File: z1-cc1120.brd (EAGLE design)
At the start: 100 x 50 mm, 8 parts, among them X1 PN61729-S

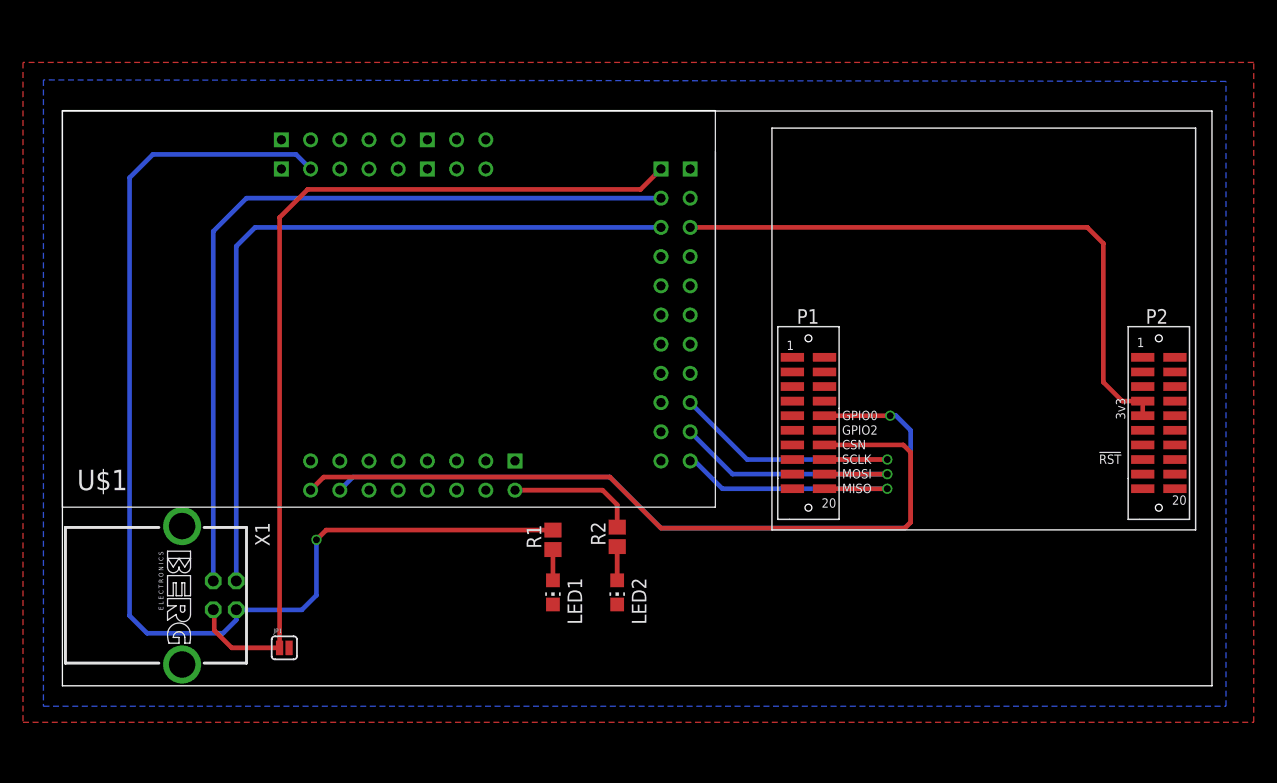
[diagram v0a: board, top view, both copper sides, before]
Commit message: Added silk screen info seperated usb_gnd & gnd added mounting holes
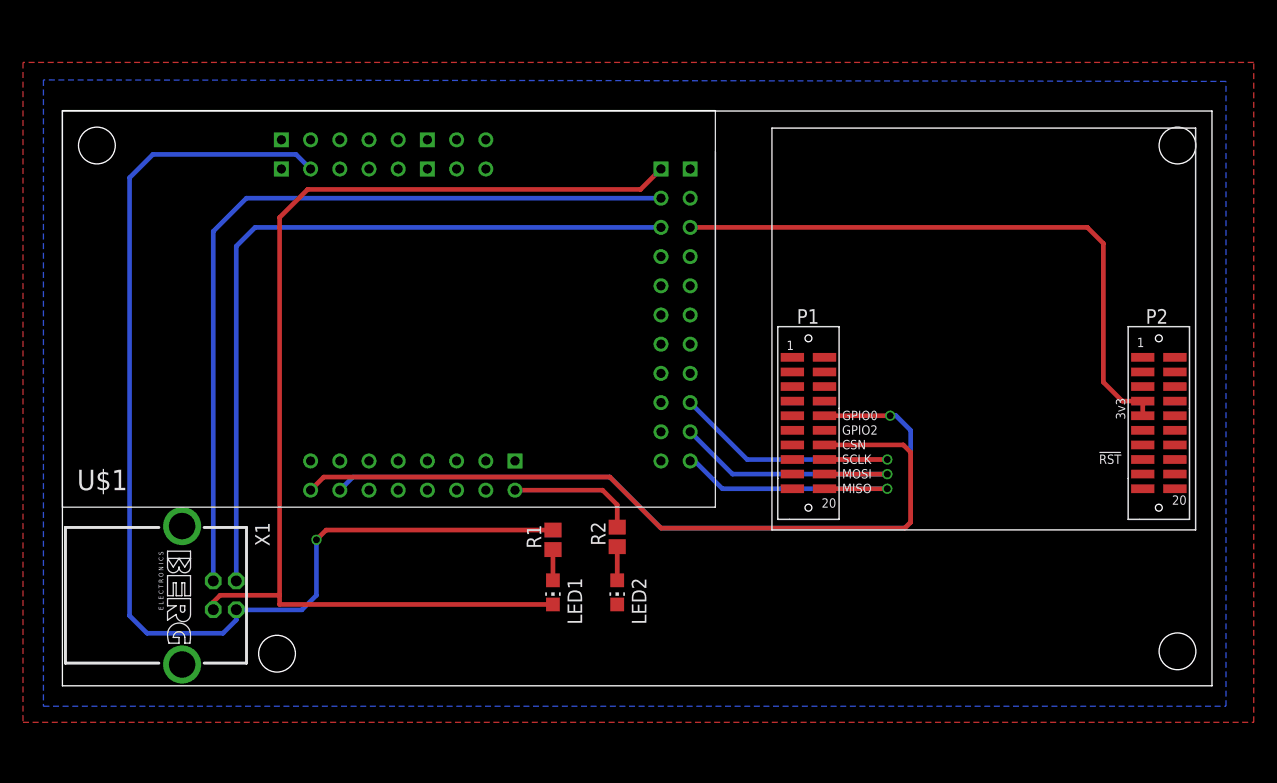
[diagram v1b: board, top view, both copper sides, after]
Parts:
- removed JP1: (no value), SparkFun-Passives:SJ_2S
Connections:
- net GND: no longer JP1.2, LED1.C
- net USB_GND: now also LED1.C; no longer JP1.1
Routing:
- net USB_GND: track 80.5 -> 99.0 mm
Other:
- board text added: "Mountain Sensing"
- board text added: "PJB"
- board text added: "Version 0.1"
- board text added: "Z1 - CC1120 Interface"
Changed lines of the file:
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@@
 <setting verticaltext="up"/>
 </settings>
-<grid distance="5" unitdist="mil" unit="mil" style="lines" multiple="1" display="no" altdistance="0.025" altunitdist="inch" altunit="inch"/>
+<grid distance="5" unitdist="mil" unit="mil" style="lines" multiple="1" display="yes" altdistance="0.025" altunitdist="inch" altunit="inch"/>
 <layers>
 <layer number="1" name="Top" color="4" fill="1" visible="yes" active="yes"/>
@@
 <layer number="43" name="vRestrict" color="2" fill="10" visible="yes" active="yes"/>
 <layer number="44" name="Drills" color="7" fill="1" visible="no" active="yes"/>
-<layer number="45" name="Holes" color="7" fill="1" visible="no" active="yes"/>
+<layer number="45" name="Holes" color="7" fill="1" visible="yes" active="yes"/>
 <layer number="46" name="Milling" color="3" fill="1" visible="no" active="yes"/>
 <layer number="47" name="Measures" color="7" fill="1" visible="no" active="yes"/>
@@
 <wire x1="100" y1="50" x2="0" y2="50" width="0" layer="20"/>
 <wire x1="0" y1="50" x2="0" y2="0" width="0" layer="20"/>
+<hole x="97" y="3" drill="3.2"/>
+<hole x="3" y="47" drill="3.2"/>
+<hole x="97" y="47" drill="3.2"/>
+<hole x="18.669" y="2.794" drill="3.2"/>
+<text x="61.087" y="9.652" size="1.778" layer="51">Z1 - CC1120 Interface</text>
+<text x="61.087" y="7.62" size="1.778" layer="51">Version 0.1</text>
+<text x="61.087" y="5.588" size="1.778" layer="51">Mountain Sensing</text>
+<text x="61.087" y="3.556" size="1.778" layer="51">PJB</text>
 </plain>
 <attributes>
@@
 <element name="LED1" library="led" package="CHIP-LED0805" value="" x="42.672" y="8.128" rot="R180"/>
 <element name="R1" library="resistor" package="R0805" value="150" x="42.672" y="12.7" rot="R90"/>
-<element name="JP1" library="SparkFun-Passives" package="SJ_2S" value="" x="19.304" y="3.302"/>
 </elements>
 <signals>
@@
 <contactref element="U$1" pad="B24" route="any" routetag="G$1.DGND"/>
 <contactref element="U$1" pad="C39" route="any" routetag="G$1.DGND"/>
-<contactref element="LED1" pad="C"/>
 <contactref element="LED2" pad="C"/>
-<contactref element="JP1" pad="2"/>
 <polygon width="0.4064" layer="16">
 <vertex x="-1.651" y="52.705"/>
@@
 <contactref element="U$1" pad="B17"/>
 <contactref element="X1" pad="4"/>
-<contactref element="JP1" pad="1"/>
-<wire x1="18.8921" y1="3.302" x2="18.8921" y2="40.7361" width="0.4064" layer="1"/>
 <wire x1="18.8921" y1="40.7361" x2="21.336" y2="43.18" width="0.4064" layer="1"/>
 <wire x1="21.336" y1="43.18" x2="50.292" y2="43.18" width="0.4064" layer="1"/>
 <wire x1="50.292" y1="43.18" x2="52.07" y2="44.958" width="0.4064" layer="1"/>
-<wire x1="18.8921" y1="3.302" x2="14.732" y2="3.302" width="0.4064" layer="1"/>
-<wire x1="14.732" y1="3.302" x2="13.208" y2="4.826" width="0.4064" layer="1"/>
-<wire x1="13.208" y1="4.826" x2="13.208" y2="6.54" width="0.4064" layer="1"/>
-<wire x1="13.208" y1="6.54" x2="13.124" y2="6.624" width="0.4064" layer="1"/>
+<contactref element="LED1" pad="C"/>
+<wire x1="18.8921" y1="40.7361" x2="18.8921" y2="7.874" width="0.4064" layer="1"/>
+<wire x1="18.8921" y1="7.874" x2="18.8921" y2="7.078" width="0.4064" layer="1"/>
+<wire x1="42.672" y1="7.078" x2="18.8921" y2="7.078" width="0.4064" layer="1"/>
+<wire x1="13.124" y1="6.624" x2="13.124" y2="7.282" width="0.4064" layer="1"/>
+<wire x1="13.124" y1="7.282" x2="13.716" y2="7.874" width="0.4064" layer="1"/>
+<wire x1="13.716" y1="7.874" x2="18.8921" y2="7.874" width="0.4064" layer="1"/>
 </signal>
 <signal name="RADIO_INT">

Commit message: Seperated radio gnd & vcc using inductor/cap network from z1 docs
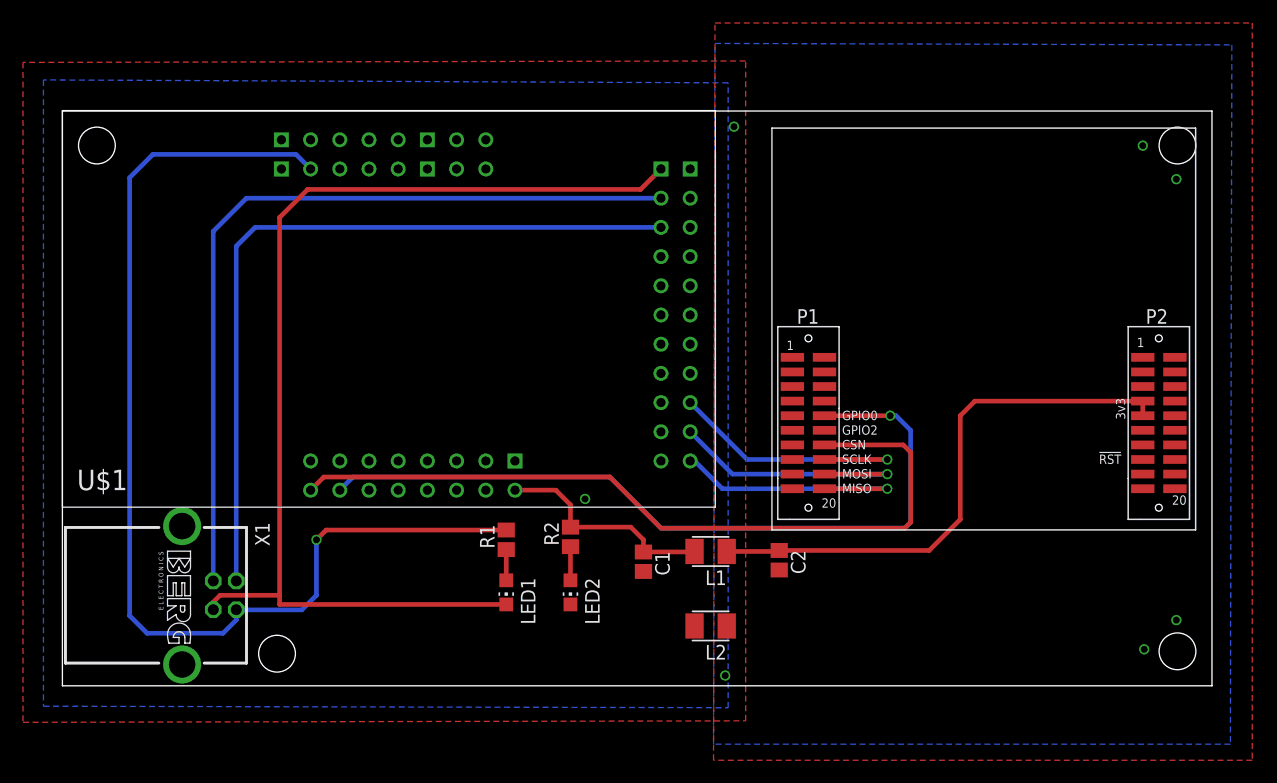
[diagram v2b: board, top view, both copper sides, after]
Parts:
- added C1, C2: 100nF, resistor:C0805
- added L1, L2: 10mH, resistor:L3230M
- moved LED1 4.06 mm to (38.6, 8.13)
- moved LED2 4.06 mm to (44.2, 8.13)
- moved R1 4.06 mm to (38.6, 12.7)
- moved R2 4.06 mm to (44.2, 13.0)
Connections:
- new net RADIO_3V3: C2.1, L1.1, U$2.3V3-1, U$2.3V3-2
- new net RADIO_GND: C2.2, L2.1, U$2.GND, U$2.GND1, U$2.GND2
- net GND: now also C1.2, L2.2; no longer U$2.GND, U$2.GND1, U$2.GND2
- net VCC_3V3: now also C1.1, L1.2; no longer U$2.3V3-1, U$2.3V3-2
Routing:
- net RADIO_3V3: track 0.00 -> 48.2 mm
- net VCC_3V3: track 65.3 -> 19.6 mm
- net USB_VCC: track 99.8 -> 95.7 mm
- net USB_GND: track 99.0 -> 95.0 mm
- added copper zone on layer 1, net RADIO_GND
- added copper zone on layer 16, net RADIO_GND
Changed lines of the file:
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@@
 <hole x="97" y="47" drill="3.2"/>
 <hole x="18.669" y="2.794" drill="3.2"/>
-<text x="61.087" y="9.652" size="1.778" layer="51">Z1 - CC1120 Interface</text>
-<text x="61.087" y="7.62" size="1.778" layer="51">Version 0.1</text>
-<text x="61.087" y="5.588" size="1.778" layer="51">Mountain Sensing</text>
-<text x="61.087" y="3.556" size="1.778" layer="51">PJB</text>
+<text x="72.898" y="9.779" size="1.778" layer="51">Z1 - CC1120 Interface</text>
+<text x="72.898" y="7.747" size="1.778" layer="51">Version 0.1</text>
+<text x="72.898" y="5.715" size="1.778" layer="51">Mountain Sensing</text>
+<text x="72.898" y="3.683" size="1.778" layer="51">PJB</text>
 </plain>
 <attributes>
@@
 <attribute name="OC_FARNELL" value="unknown" x="10.414" y="7.874" size="1.778" layer="27" rot="R270" display="off"/>
 </element>
-<element name="LED2" library="led" package="CHIP-LED0805" value="" x="48.26" y="8.128" rot="R180"/>
-<element name="R2" library="resistor" package="R0805" value="56" x="48.26" y="12.954" rot="R90"/>
-<element name="LED1" library="led" package="CHIP-LED0805" value="" x="42.672" y="8.128" rot="R180"/>
-<element name="R1" library="resistor" package="R0805" value="150" x="42.672" y="12.7" rot="R90"/>
+<element name="LED2" library="led" package="CHIP-LED0805" value="" x="44.196" y="8.128" rot="R180"/>
+<element name="R2" library="resistor" package="R0805" value="56" x="44.196" y="12.954" rot="R90"/>
+<element name="LED1" library="led" package="CHIP-LED0805" value="" x="38.608" y="8.128" rot="R180"/>
+<element name="R1" library="resistor" package="R0805" value="150" x="38.608" y="12.7" rot="R90"/>
+<element name="C1" library="resistor" package="C0805" value="100nF" x="50.546" y="10.795" rot="R270"/>
+<element name="C2" library="resistor" package="C0805" value="100nF" x="62.357" y="10.922" rot="R270"/>
+<element name="L1" library="resistor" package="L3230M" value="10mH" x="56.388" y="11.684" rot="R180"/>
+<element name="L2" library="resistor" package="L3230M" value="10mH" x="56.388" y="5.207" rot="R180"/>
 </elements>
 <signals>
@@
 <contactref element="U$1" pad="C39" route="any" routetag="G$1.DGND"/>
 <contactref element="LED2" pad="C"/>
-<polygon width="0.4064" layer="16">
+<polygon width="0.4064" layer="16" rank="2">
 <vertex x="-1.651" y="52.705"/>
 <vertex x="-1.651" y="-1.778"/>
-<vertex x="101.219" y="-1.778"/>
-<vertex x="101.219" y="52.578"/>
+<vertex x="57.912" y="-1.905"/>
+<vertex x="57.912" y="52.451"/>
 </polygon>
-<polygon width="0.4064" layer="1">
+<polygon width="0.4064" layer="1" rank="2">
 <vertex x="-3.429" y="54.229"/>
 <vertex x="-3.429" y="-3.175"/>
-<vertex x="103.632" y="-3.175"/>
-<vertex x="103.632" y="54.229"/>
+<vertex x="59.436" y="-3.048"/>
+<vertex x="59.436" y="54.356"/>
 </polygon>
-<contactref element="U$2" pad="GND"/>
-<contactref element="U$2" pad="GND1"/>
-<contactref element="U$2" pad="GND2"/>
+<contactref element="C1" pad="2"/>
+<contactref element="L2" pad="2"/>
+<via x="45.466" y="16.256" extent="1-16" drill="0.6" shape="octagon"/>
 </signal>
 <signal name="VCC_3V3">
@@
 <contactref element="U$1" pad="C40" route="any" routetag="G$1.D-3V"/>
 <contactref element="R2" pad="2"/>
-<contactref element="U$2" pad="3V3-1"/>
-<contactref element="U$2" pad="3V3-2"/>
-<wire x1="39.37" y1="17.018" x2="46.99" y2="17.018" width="0.4064" layer="1"/>
-<wire x1="46.99" y1="17.018" x2="48.26" y2="15.748" width="0.4064" layer="1"/>
-<wire x1="48.26" y1="15.748" x2="48.26" y2="13.804" width="0.4064" layer="1"/>
-<wire x1="54.61" y1="39.878" x2="89.154" y2="39.878" width="0.4064" layer="1"/>
-<wire x1="89.154" y1="39.878" x2="90.551" y2="38.481" width="0.4064" layer="1"/>
-<wire x1="90.551" y1="38.481" x2="90.551" y2="26.416" width="0.4064" layer="1"/>
-<wire x1="90.551" y1="26.416" x2="92.202" y2="24.765" width="0.4064" layer="1"/>
-<wire x1="92.202" y1="24.765" x2="93.98" y2="24.765" width="0.4064" layer="1"/>
-<wire x1="93.98" y1="24.765" x2="93.98" y2="23.495" width="0.4064" layer="1"/>
+<wire x1="39.37" y1="17.018" x2="42.926" y2="17.018" width="0.4064" layer="1"/>
+<wire x1="42.926" y1="17.018" x2="44.196" y2="15.748" width="0.4064" layer="1"/>
+<wire x1="44.196" y1="15.748" x2="44.196" y2="13.804" width="0.4064" layer="1"/>
+<contactref element="L1" pad="2"/>
+<contactref element="C1" pad="1"/>
+<wire x1="44.196" y1="13.804" x2="49.442" y2="13.804" width="0.4064" layer="1"/>
+<wire x1="49.442" y1="13.804" x2="50.546" y2="12.7" width="0.4064" layer="1"/>
+<wire x1="50.546" y1="12.7" x2="50.546" y2="11.645" width="0.4064" layer="1"/>
+<wire x1="50.546" y1="11.645" x2="54.949" y2="11.645" width="0.4064" layer="1"/>
+<wire x1="54.949" y1="11.645" x2="54.988" y2="11.684" width="0.4064" layer="1"/>
 </signal>
 <signal name="SPI_CLK">
@@
 <wire x1="7.874" y1="46.228" x2="20.32" y2="46.228" width="0.4064" layer="16"/>
 <wire x1="20.32" y1="46.228" x2="21.59" y2="44.958" width="0.4064" layer="16"/>
-<wire x1="42.672" y1="13.55" x2="22.948" y2="13.55" width="0.4064" layer="1"/>
+<wire x1="38.608" y1="13.55" x2="22.948" y2="13.55" width="0.4064" layer="1"/>
 <wire x1="22.948" y1="13.55" x2="22.098" y2="12.7" width="0.4064" layer="1"/>
 <via x="22.098" y="12.7" extent="1-16" drill="0.6"/>
@@
 <wire x1="18.8921" y1="40.7361" x2="18.8921" y2="7.874" width="0.4064" layer="1"/>
 <wire x1="18.8921" y1="7.874" x2="18.8921" y2="7.078" width="0.4064" layer="1"/>
-<wire x1="42.672" y1="7.078" x2="18.8921" y2="7.078" width="0.4064" layer="1"/>
+<wire x1="38.608" y1="7.078" x2="18.8921" y2="7.078" width="0.4064" layer="1"/>
 <wire x1="13.124" y1="6.624" x2="13.124" y2="7.282" width="0.4064" layer="1"/>
 <wire x1="13.124" y1="7.282" x2="13.716" y2="7.874" width="0.4064" layer="1"/>
@@
 <contactref element="LED2" pad="A"/>
 <contactref element="R2" pad="1"/>
-<wire x1="48.26" y1="12.104" x2="48.26" y2="9.178" width="0.4064" layer="1"/>
+<wire x1="44.196" y1="12.104" x2="44.196" y2="9.178" width="0.4064" layer="1"/>
 </signal>
 <signal name="N$26">
 <contactref element="LED1" pad="A"/>
 <contactref element="R1" pad="1"/>
-<wire x1="42.672" y1="11.85" x2="42.672" y2="9.178" width="0.4064" layer="1"/>
+<wire x1="38.608" y1="11.85" x2="38.608" y2="9.178" width="0.4064" layer="1"/>
 </signal>
 <signal name="VCC-3V">
@@
 <contactref element="U$1" pad="A4" route="any" routetag="G$1.ADC_3V3"/>
 </signal>
+<signal name="RADIO_GND">
+<contactref element="U$2" pad="GND"/>
+<contactref element="U$2" pad="GND1"/>
+<contactref element="U$2" pad="GND2"/>
+<contactref element="L2" pad="1"/>
+<contactref element="C2" pad="2"/>
+<polygon width="0.4064" layer="1">
+<vertex x="103.505" y="57.658"/>
+<vertex x="103.505" y="-6.477"/>
+<vertex x="56.642" y="-6.477"/>
+<vertex x="56.769" y="57.658"/>
+</polygon>
+<polygon width="0.4064" layer="16">
+<vertex x="101.727" y="55.753"/>
+<vertex x="101.6" y="-5.08"/>
+<vertex x="56.642" y="-5.08"/>
+<vertex x="56.769" y="55.88"/>
+</polygon>
+<via x="57.658" y="0.889" extent="1-16" drill="0.6" shape="octagon"/>
+<via x="58.42" y="48.641" extent="1-16" drill="0.6" shape="octagon"/>
+<via x="96.901" y="44.069" extent="1-16" drill="0.6" shape="octagon"/>
+<via x="93.98" y="46.99" extent="1-16" drill="0.6" shape="octagon"/>
+<via x="94.107" y="3.175" extent="1-16" drill="0.6" shape="octagon"/>
+<via x="96.901" y="5.715" extent="1-16" drill="0.6" shape="octagon"/>
+</signal>
+<signal name="RADIO_3V3">
+<contactref element="U$2" pad="3V3-1"/>
+<contactref element="U$2" pad="3V3-2"/>
+<wire x1="93.98" y1="24.765" x2="93.98" y2="23.495" width="0.4064" layer="1"/>
+<contactref element="L1" pad="1"/>
+<contactref element="C2" pad="1"/>
+<wire x1="57.788" y1="11.684" x2="62.269" y2="11.684" width="0.4064" layer="1"/>
+<wire x1="62.269" y1="11.684" x2="62.357" y2="11.772" width="0.4064" layer="1"/>
+<wire x1="62.357" y1="11.772" x2="75.399" y2="11.772" width="0.4064" layer="1"/>
+<wire x1="75.399" y1="11.772" x2="78.105" y2="14.478" width="0.4064" layer="1"/>
+<wire x1="78.105" y1="14.478" x2="78.105" y2="23.495" width="0.4064" layer="1"/>
+<wire x1="78.105" y1="23.495" x2="79.375" y2="24.765" width="0.4064" layer="1"/>
+<wire x1="79.375" y1="24.765" x2="93.98" y2="24.765" width="0.4064" layer="1"/>
+</signal>
 </signals>
